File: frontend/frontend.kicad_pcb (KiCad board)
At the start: 2 copper layers, 32.5 x 22.5 mm, 50 parts, among them Q1 T2N7002AK,LM, Q2 NX3008PBK,215, Q3 NX3008PBK,215, Q4 T2N7002AK,LM, Q5 NX3008PBK,215, Q6 T2N7002AK,LM, U1 ADS1291/2, U2 KC2016Z2

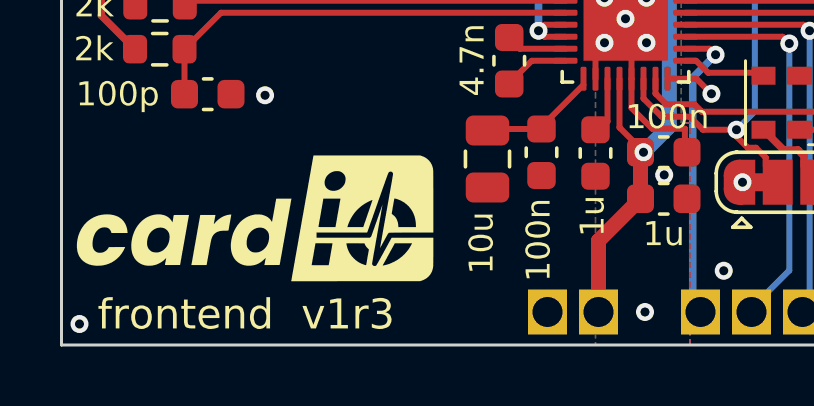
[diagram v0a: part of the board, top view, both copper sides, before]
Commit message: Remove battery ADC parts, simplify and tweak routing, add locking holes to jtag
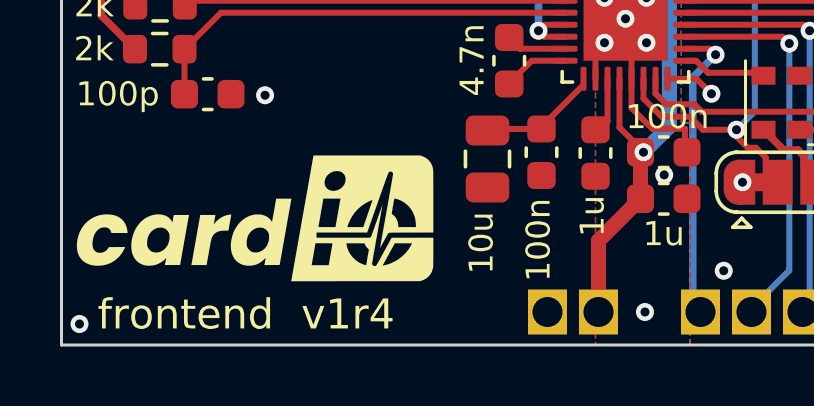
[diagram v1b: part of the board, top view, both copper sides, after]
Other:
- board text added: "v1r4"
- board text removed: "v1r3"
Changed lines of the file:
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@@
     (effects (font (size 1 1) (thickness 0.15)) (justify left bottom))
   )
-  (gr_text "v1r3" (at 118.49 82.57) (layer "F.SilkS")
+  (gr_text "v1r4" (at 118.49 82.57) (layer "F.SilkS")
     (effects (font (size 1 1) (thickness 0.15)) (justify left bottom))
   )

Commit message: Finalize v1r4
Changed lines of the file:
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@@
   (segment (start 132.1645 74.6255) (end 131.664 74.125) (width 0.2) (layer "F.Cu") (net 4))
   (segment (start 131.664 74.125) (end 130.7 74.125) (width 0.2) (layer "F.Cu") (net 4))
-  (via (at 137.5 74.3) (size 0.6) (drill 0.3) (layers "F.Cu" "B.Cu") (free) (net 4))
+  (via (at 136.95 74.35) (size 0.6) (drill 0.3) (layers "F.Cu" "B.Cu") (free) (net 4))
   (via (at 134.3 68.125) (size 0.6) (drill 0.3) (layers "F.Cu" "B.Cu") (free) (net 4))
   (via (at 140.7 76.3) (size 0.6) (drill 0.3) (layers "F.Cu" "B.Cu") (free) (net 4))

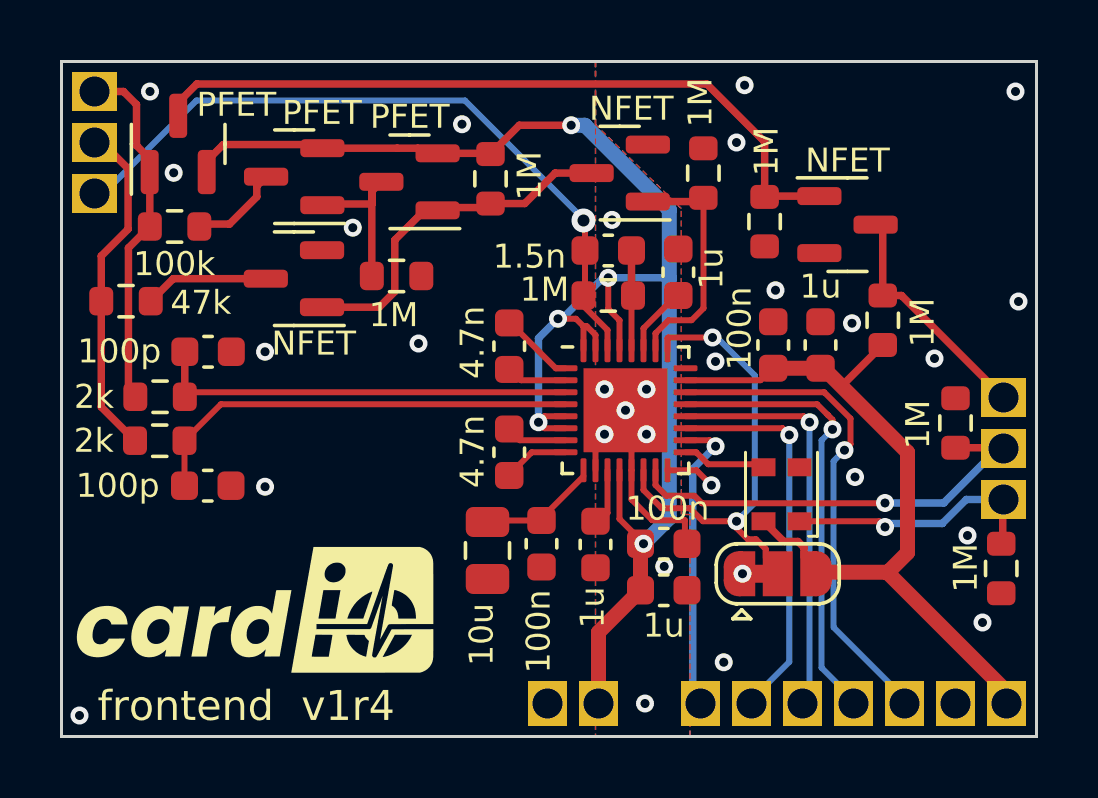
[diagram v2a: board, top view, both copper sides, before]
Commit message: Close #31: tweak touch detection
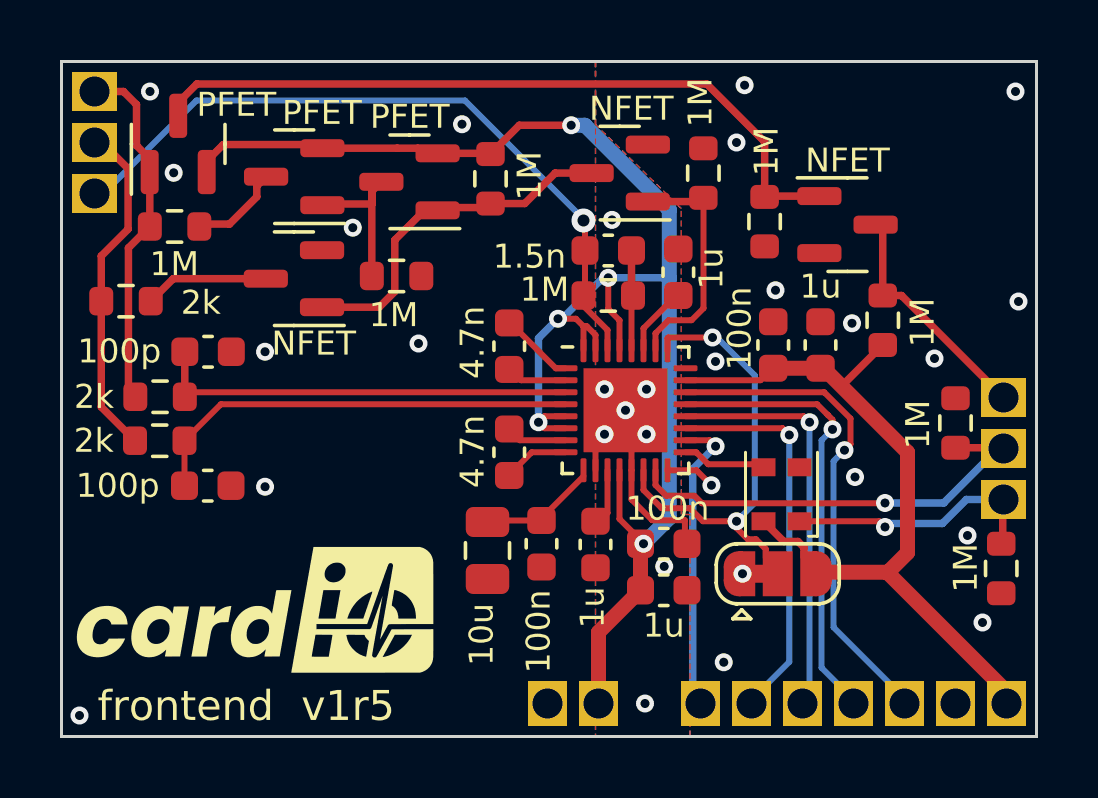
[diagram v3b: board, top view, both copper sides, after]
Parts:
- R12: value 47k -> 2k
- R3: value 100k -> 1M
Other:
- board text added: "v1r5"
- board text removed: "v1r4"
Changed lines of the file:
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@@
         (effects (font (size 1 1) (thickness 0.15)))
     )
-    (fp_text value "47k" (at -2.495 -0.05) (layer "F.SilkS")
+    (fp_text value "2k" (at -2.495 -0.05) (layer "F.SilkS")
         (effects (font (size 0.8 0.8) (thickness 0.1)))
     )
@@
         (effects (font (size 1 1) (thickness 0.15)))
     )
-    (fp_text value "100k" (at -0.01 1.25) (layer "F.SilkS")
+    (fp_text value "1M" (at -0.01 1.25) (layer "F.SilkS")
         (effects (font (size 0.8 0.8) (thickness 0.1)))
     )
@@
     (effects (font (size 1 1) (thickness 0.15)) (justify left bottom))
   )
-  (gr_text "v1r4" (at 118.49 82.57) (layer "F.SilkS")
+  (gr_text "v1r5" (at 118.49 82.57) (layer "F.SilkS")
     (effects (font (size 1 1) (thickness 0.15)) (justify left bottom))
   )

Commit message: Tweak touch detector circuit
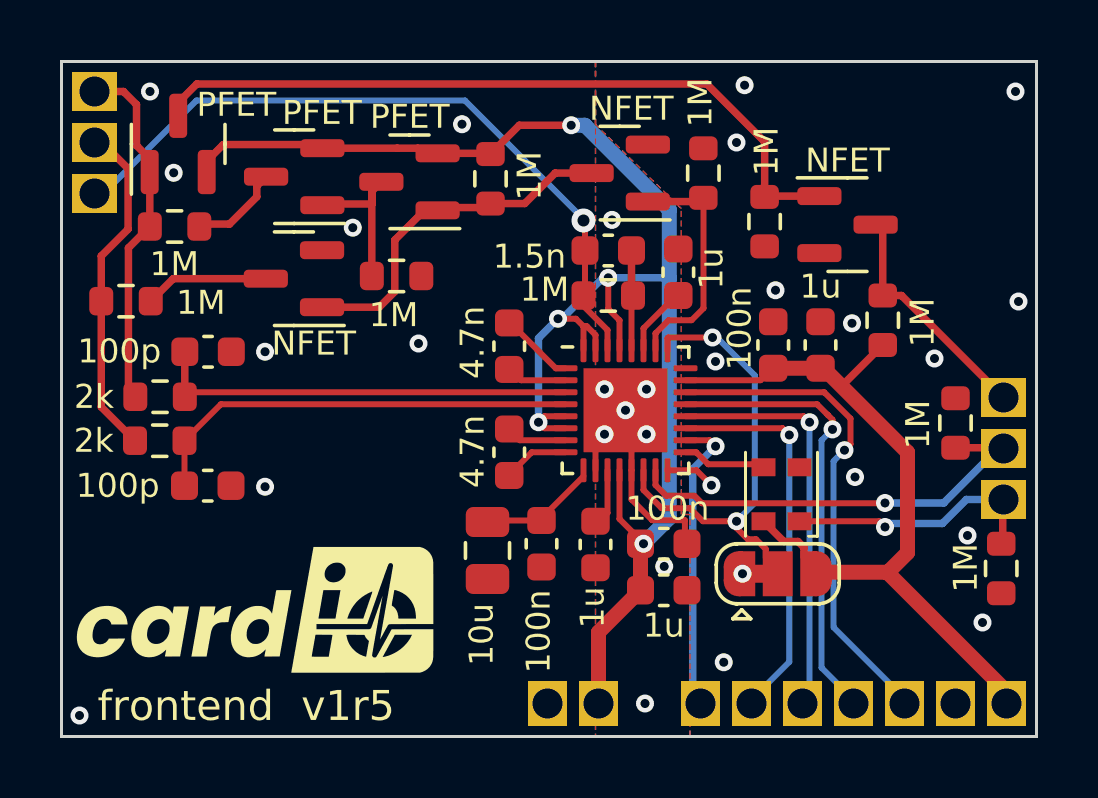
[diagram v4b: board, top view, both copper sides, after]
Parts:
- R12: value 2k -> 1M
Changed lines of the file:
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@@
         (effects (font (size 1 1) (thickness 0.15)))
     )
-    (fp_text value "2k" (at -2.495 -0.05) (layer "F.SilkS")
+    (fp_text value "1M" (at -2.495 -0.05) (layer "F.SilkS")
         (effects (font (size 0.8 0.8) (thickness 0.1)))
     )

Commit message: Shrink frontend a bit
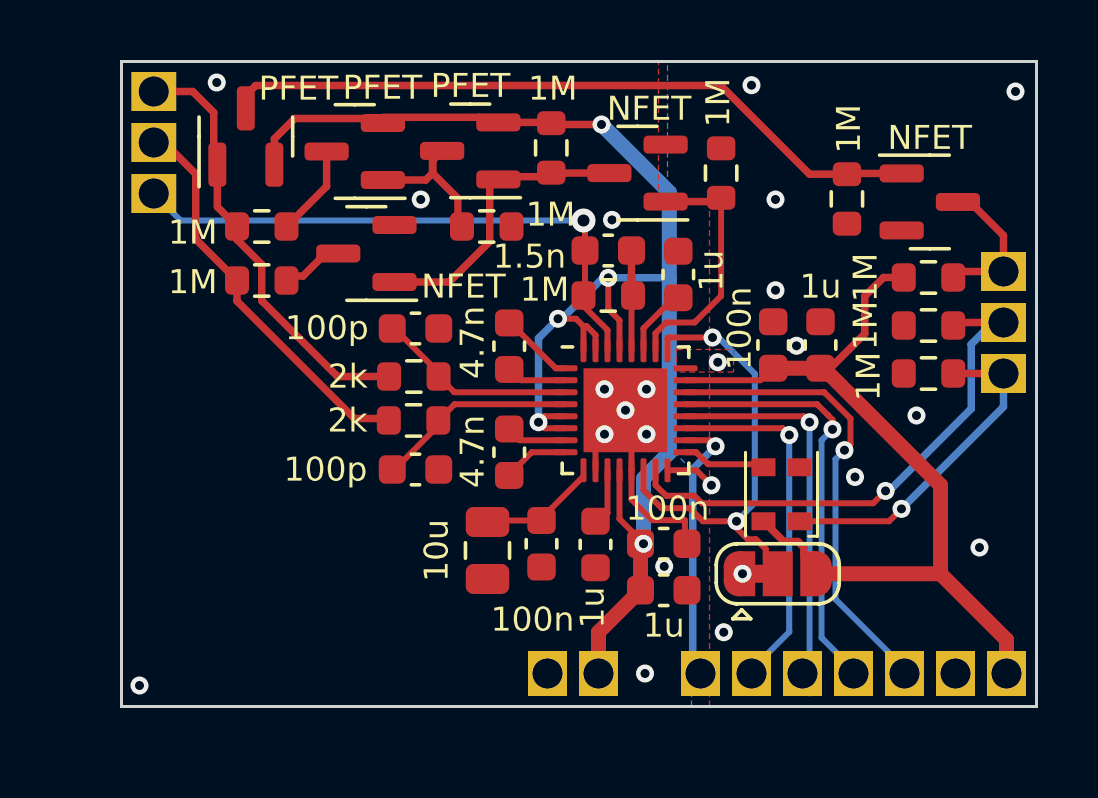
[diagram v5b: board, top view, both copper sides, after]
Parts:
- G1: moved to B.Cu
- moved R1 8.49 mm to (122.2, 71.0)
- moved R2 8.49 mm to (122.2, 72.5)
- moved C11 6.96 mm to (122.3, 69.4)
- moved C12 6.95 mm to (122.3, 74.1)
- moved R4 6.94 mm to (139.4, 70.9), turned to 0 degrees
- moved R12 4.58 mm to (117.2, 67.8)
- moved ~{RESET}/~{PDN}1 4.20 mm to (141.9, 69.2)
- moved ~{TOUCH_DET}1 4.20 mm to (141.9, 67.5)
- moved CLK_EN1 4.20 mm to (141.9, 70.9)
- moved R9 3.43 mm to (124.7, 66.0)
- moved R16 3.37 mm to (139.4, 69.3), turned to 0 degrees
- moved R3 2.91 mm to (117.2, 66.0)
- moved R13 2.85 mm to (136.7, 65.1)
- moved Q6 2.85 mm to (139.4, 65.2)
- moved Q4 2.56 mm to (120.7, 66.9)
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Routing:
- net Net-(U1-IN1P): track 14.7 -> 6.34 mm
- net Net-(U1-IN1N): track 14.0 -> 6.38 mm
- net /VGND: track 25.2 -> 20.6 mm
- net Net-(Q6-D): track 7.89 -> 3.86 mm
- net Net-(Q4-D): track 4.15 -> 1.46 mm
- net Net-(U1-~{PDN}/~{RESET}): track 14.8 -> 17.4 mm
- net Net-(Q5-G): track 11.8 -> 14.2 mm
- net Net-(U2-INH): track 8.68 -> 11.2 mm
- net +BATT: track 52.1 -> 49.7 mm
- net +3.3V: track 25.5 -> 27.5 mm
- net /TOFF: track 10.9 -> 8.92 mm
- net Net-(ECG_R1-Pad1): track 11.3 -> 12.9 mm
- net Net-(U1-~{CS}): track 9.82 -> 8.72 mm
- net Net-(U1-~{DRDY}): track 16.3 -> 15.2 mm
- net Net-(Q5-D): track 24.2 -> 23.2 mm
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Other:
- board size 32.5 x 22.5 mm -> 30.5 x 21.5 mm

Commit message: Add second channel components
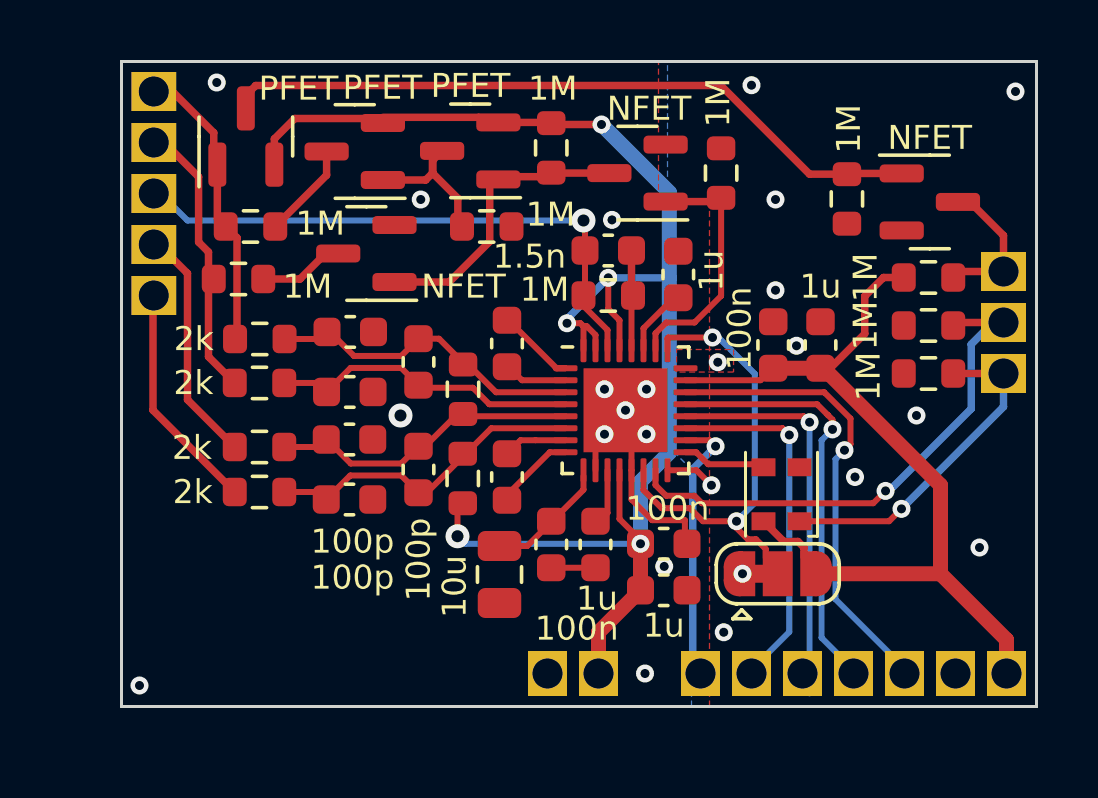
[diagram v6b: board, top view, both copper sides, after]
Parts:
- added C13: 100p, Capacitor_SMD:C_0603_1608Metric, F.Cu at (120.1, 73.1)
- added C14: 100p, Capacitor_SMD:C_0603_1608Metric, F.Cu at (120.1, 75.1)
- added C15: 100p, Capacitor_SMD:C_0603_1608Metric, F.Cu at (122.4, 74.1)
- added C17: 100p, Capacitor_SMD:C_0603_1608Metric, F.Cu at (122.4, 70.5)
- added ECG3: ~, frontend_parts:PAD, F.Cu at (113.6, 66.6)
- added ECG4: ~, frontend_parts:PAD, F.Cu at (113.6, 68.3)
- added R15: 0R, Resistor_SMD:R_0603_1608Metric, F.Cu at (123.9, 74.4)
- added R5: 2k, Resistor_SMD:R_0603_1608Metric, F.Cu at (117.1, 73.3)
- added R6: 2k, Resistor_SMD:R_0603_1608Metric, F.Cu at (117.1, 74.8)
- added R7: 0R, Resistor_SMD:R_0603_1608Metric, F.Cu at (123.9, 71.4)
- moved R1 5.28 mm to (117.1, 69.8)
- moved R2 5.28 mm to (117.1, 71.2)
- moved C12 3.39 mm to (120.1, 71.5)
- moved C11 2.18 mm to (120.1, 69.5)
- moved C9 0.89 mm to (125.1, 77.6)
- moved C5 0.83 mm to (125.3, 74.3)
- moved R12 0.78 mm to (116.4, 67.8)
- moved R3 0.38 mm to (116.8, 66.0)
- moved C10 0.33 mm to (126.8, 76.6)
- moved C6 0.12 mm to (125.3, 69.9)
- renumbered ECG_L1 to ECG1, ECG_R1 to ECG2
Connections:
- net Net-(U1-IN1N) renamed /ECG1N
- net Net-(U1-IN1P) renamed /ECG1P
- U1 pad 5: +BATT -> /ECG2N
- U1 pad 6: +BATT -> /ECG2P
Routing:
- net /ECG2P: track 0.00 -> 11.1 mm
- net /ECG2N: track 0.00 -> 10.6 mm
- net Net-(ECG3-Pad1): track 0.00 -> 7.99 mm
- net Net-(ECG4-Pad1): track 0.00 -> 7.68 mm
- net Net-(Q5-G): track 14.2 -> 9.52 mm
- net /ECG1N: track 6.38 -> 10.8 mm
- net /ECG1P: track 6.34 -> 10.4 mm
- net Net-(ECG2-Pad1): track 12.9 -> 8.99 mm
- net GNDA: track 6.56 -> 8.03 mm, vias 11 -> 12
- net Net-(Q4-D): track 1.46 -> 2.38 mm
- net +BATT: track 49.7 -> 50.6 mm
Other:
- board text added: "ECG1(L)"
- board text added: "ECG2(R)"
- board text added: "ECG3"
- board text added: "ECG4"
- board text removed: "ECG_L"
- board text removed: "ECG_R"

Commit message: Tweak frontend
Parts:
- moved R7 6.86 mm to (117.1, 72.2), turned to 0 degrees
- moved R6 0.55 mm to (117.1, 75.4)
- moved R1 0.53 mm to (117.1, 69.2)
- moved R5 0.48 mm to (117.1, 73.8)
- moved R2 0.44 mm to (117.1, 70.8)
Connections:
- net /ECG1P renamed Net-(U1-IN1P)
- net Net-(ECG2-Pad1) renamed /R
- net Net-(ECG4-Pad1) renamed /LL
- C11 pad 1: /ECG1N -> Net-(U1-IN1N)
- C13 pad 1: /ECG2N -> Net-(U1-IN2N)
- C15 pad 1: /ECG2N -> Net-(U1-IN2N)
- C17 pad 1: /ECG1N -> Net-(U1-IN1N)
- ECG1 pad 1: Net-(Q5-G) -> /L
- ECG3 pad 1: Net-(ECG3-Pad1) -> /L2
- Q5 pad 1: Net-(Q5-G) -> /L
- R1 pad 1: Net-(Q5-G) -> /L
- R1 pad 2: /ECG1N -> Net-(U1-IN1N)
- R3 pad 1: Net-(Q5-G) -> /L
- R5 pad 1: Net-(ECG3-Pad1) -> /L2
- R5 pad 2: /ECG2N -> Net-(U1-IN2N)
- R7 pad 1: /ECG1N -> /L2
- R7 pad 2: /ECG2N -> /L
- U1 pad 3: /ECG1N -> Net-(U1-IN1N)
- U1 pad 5: /ECG2N -> Net-(U1-IN2N)
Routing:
- net /L: track 0.00 -> 12.4 mm
- net /ECG1N: track 10.8 -> 0.00 mm
- net Net-(U1-IN1N): track 0.00 -> 10.8 mm
- net /ECG2N: track 10.6 -> 0.00 mm
- net Net-(U1-IN2N): track 0.00 -> 10.5 mm
- net /L2: track 0.00 -> 9.80 mm
- net Net-(Q5-G): track 9.52 -> 0.00 mm
- net Net-(ECG3-Pad1): track 7.99 -> 0.00 mm
- net /ECG2P: track 11.1 -> 10.4 mm
- net /LL: track 7.68 -> 8.23 mm

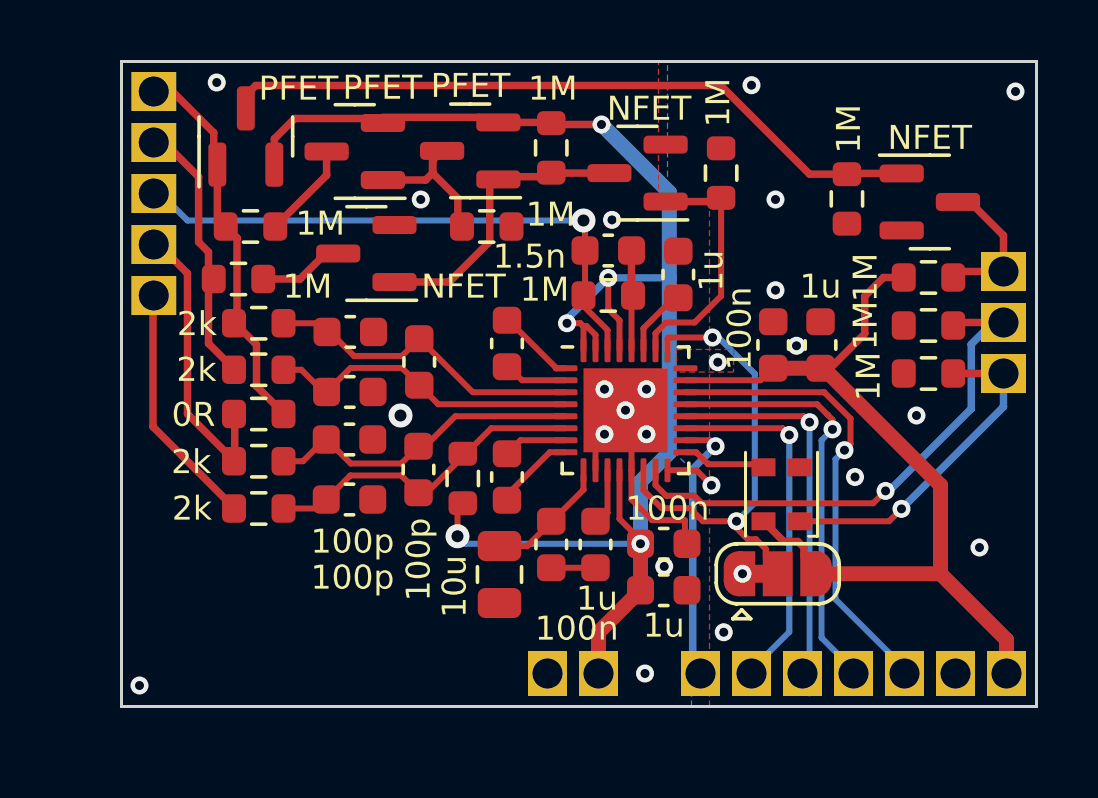
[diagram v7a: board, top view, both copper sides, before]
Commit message: Final tweaks: switch ch2 electrodes
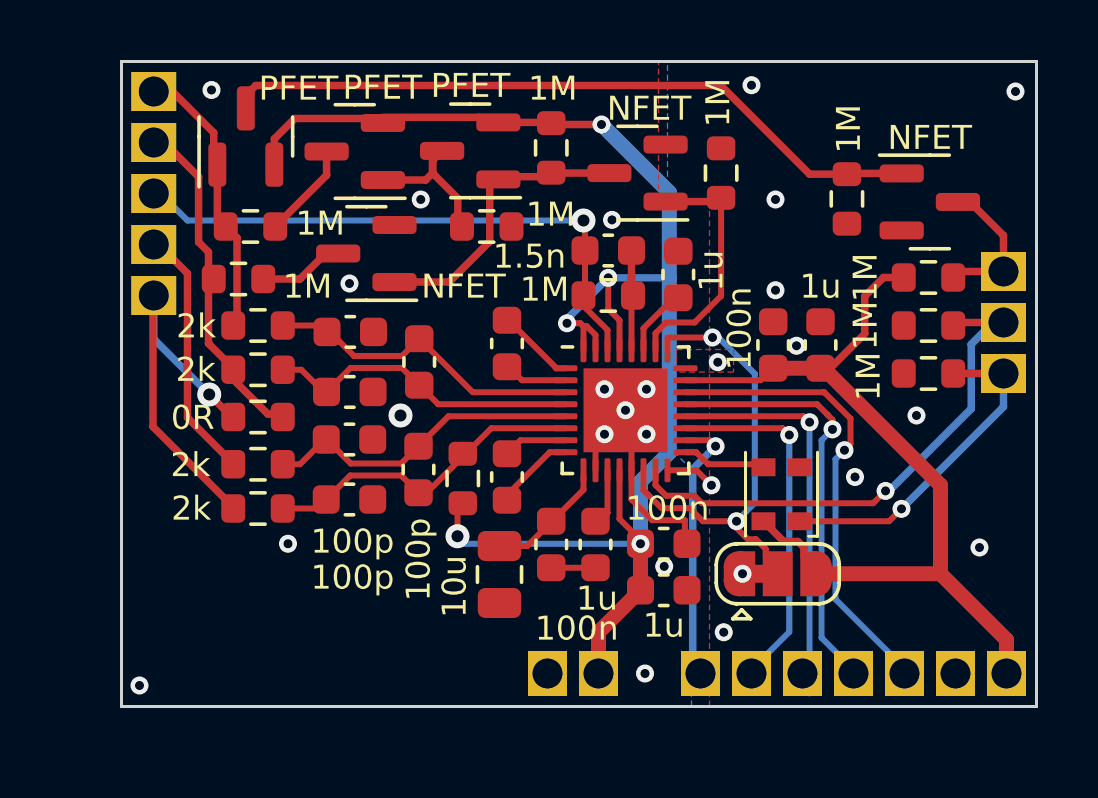
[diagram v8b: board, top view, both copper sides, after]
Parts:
- moved R5 0.10 mm to (117.0, 73.9)
- moved R7 0.10 mm to (117.0, 72.3)
- moved R1 0.08 mm to (117.0, 69.3)
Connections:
- ECG3 pad 1: /L2 -> /LL
- ECG4 pad 1: /LL -> /R2
- R5 pad 1: /L2 -> /LL
- R6 pad 1: /LL -> /R2
- R7 pad 1: /L2 -> /R2
- R7 pad 2: /L -> /R
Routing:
- net /R2: track 0.00 -> 13.4 mm, vias 0 -> 1
- net /L2: track 9.80 -> 0.00 mm
- net /L: track 12.4 -> 8.67 mm
- net /R: track 8.55 -> 10.7 mm
- net GNDA: vias 12 -> 14
